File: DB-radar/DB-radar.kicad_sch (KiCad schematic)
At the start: 33 parts, among them J1 Conn_01x10_Female, J2 USB_C_Receptacle, Q1 FS8205A, SW1 SW_Push, U1 ATmega328PB-A, U2 DW01A-G, U3 TP4056, U4 XC6206PxxxMR, Y1 Crystal_GND3_Small

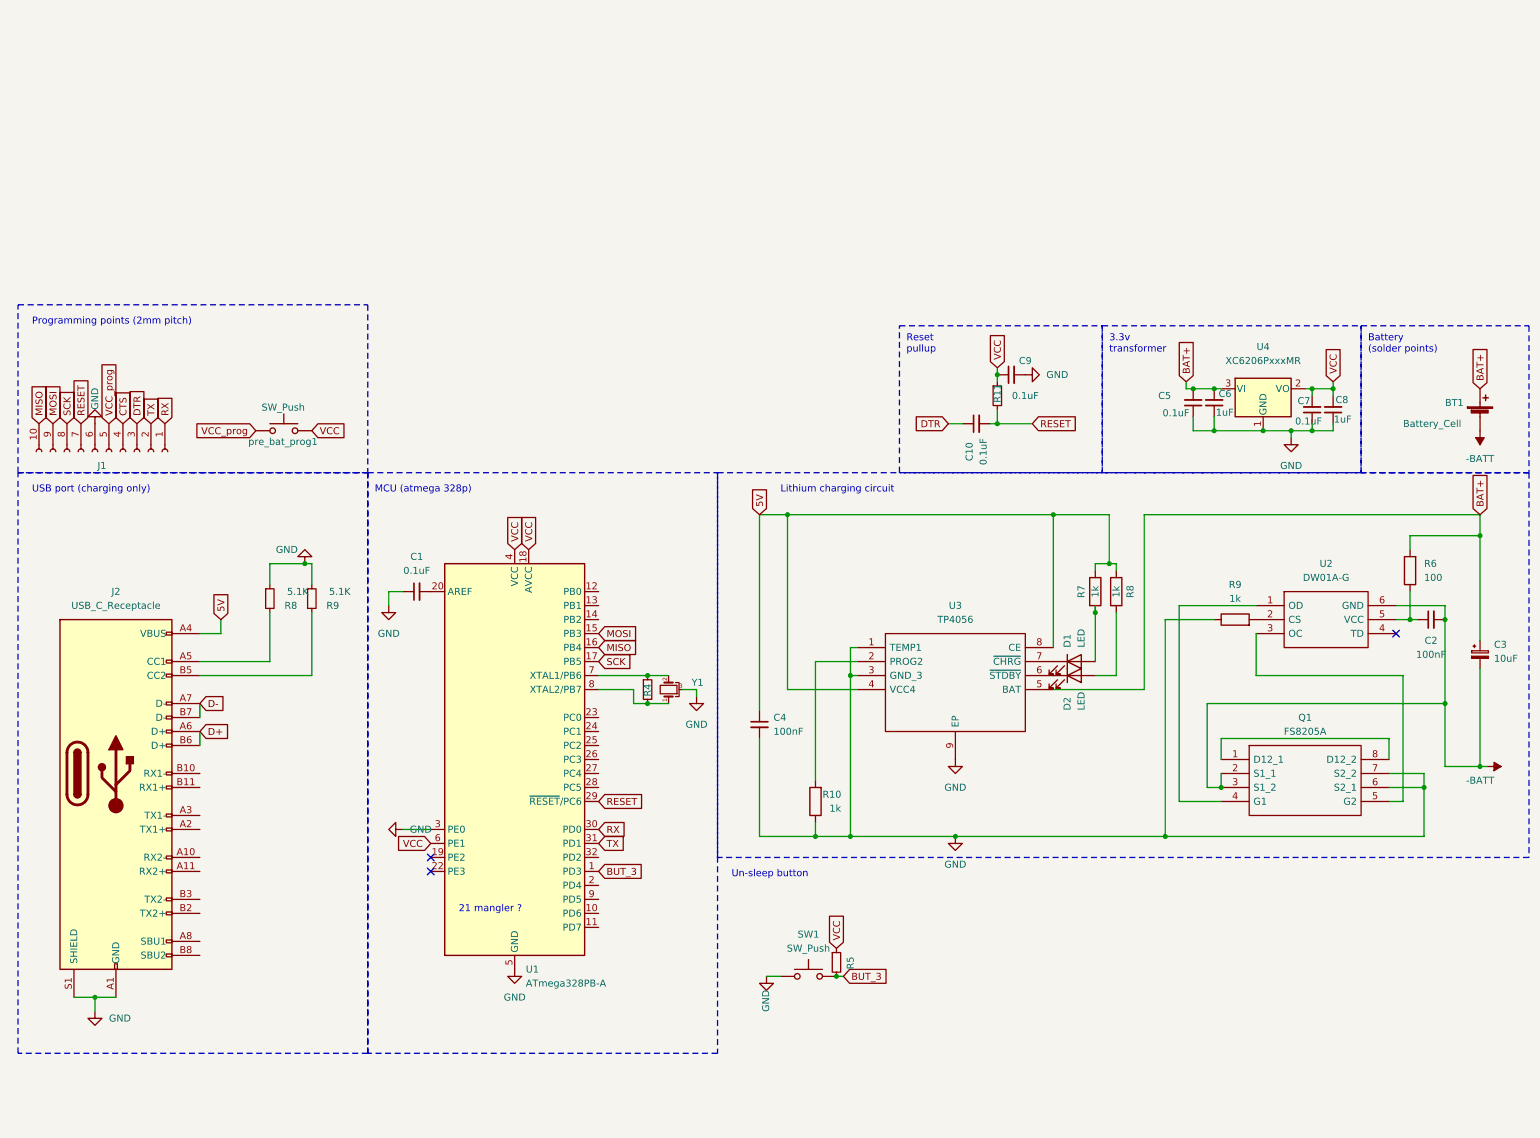
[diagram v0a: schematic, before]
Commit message: Added LED and multiplexers and started PCB design
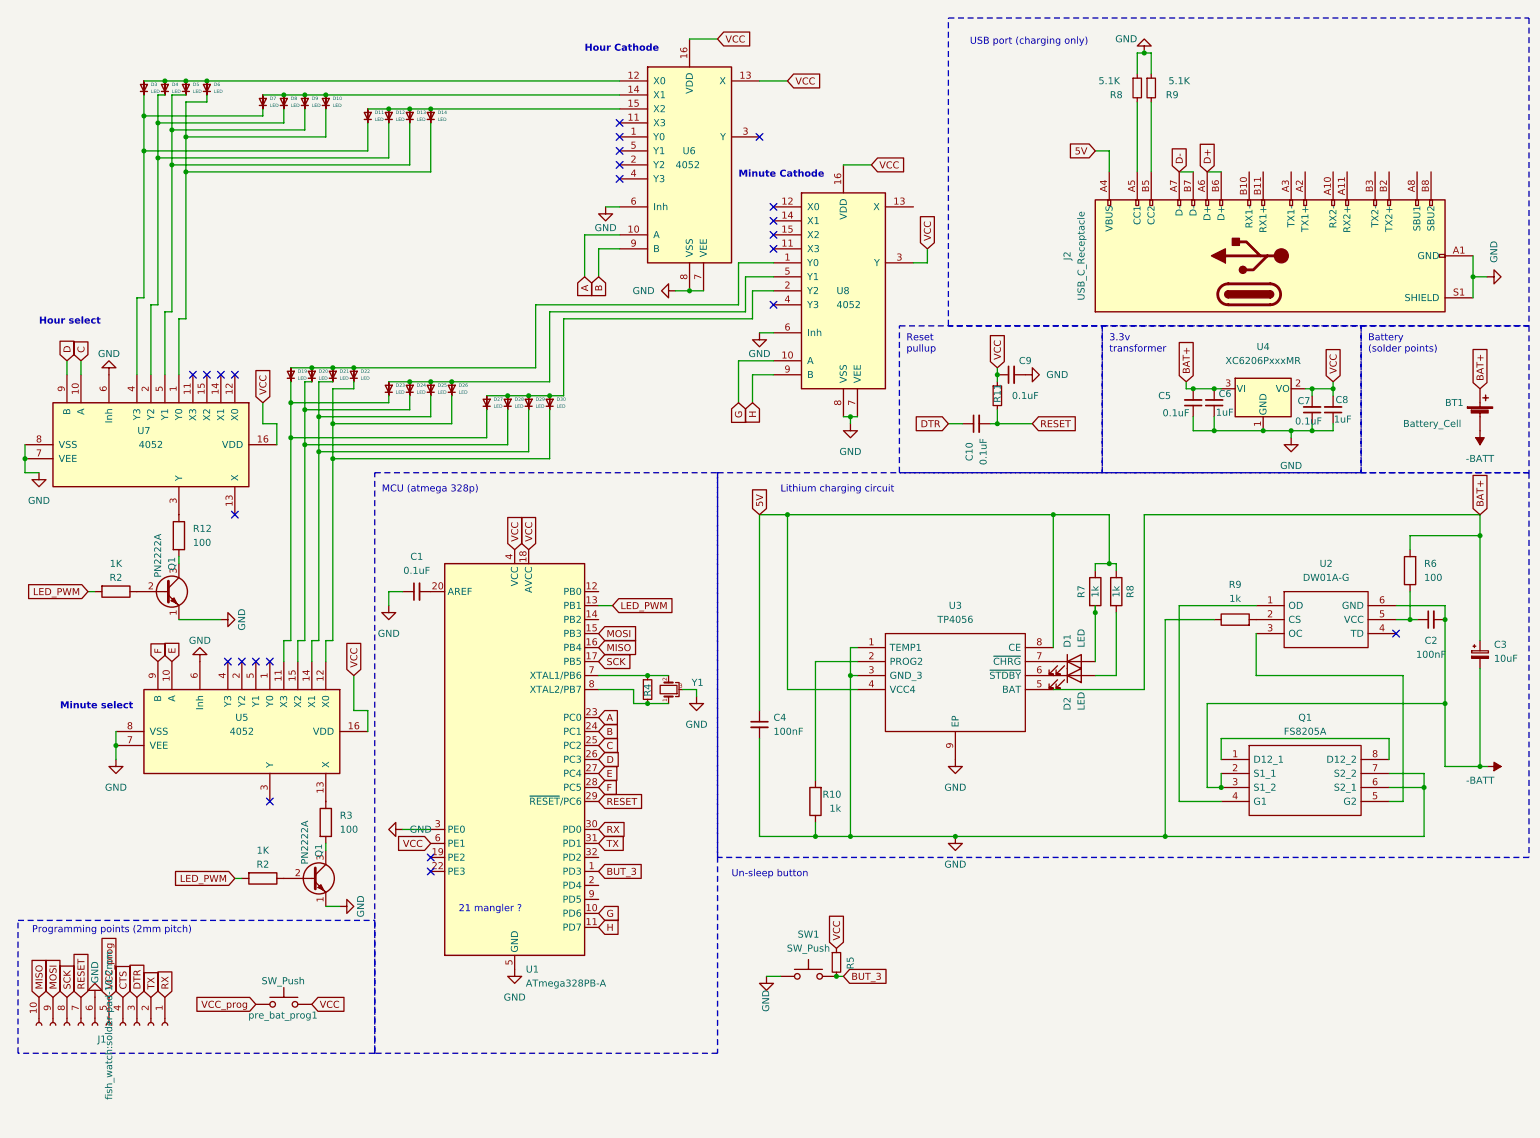
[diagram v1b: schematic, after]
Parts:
- added D10, D11, D12, D13, D14, D19, D20, D21, D22, D23, D24, D25, D26, D27, D28, D29, D3, D30, D4, D5, D6, D7, D8, D9: LED, LED_SMD:LED_0805_2012Metric, symbol Device:LED
- added Q1 (x2): PN2222A, transistorer:MMBT2222A, symbol Transistor_BJT:PN2222A
- added R12, R3: 100, Resistor_SMD:R_0603_1608Metric, symbol Device:R
- added R2 (x2): 1K, Resistor_SMD:R_0603_1608Metric, symbol Device:R
- added U5, U6, U7, U8: 4052, Package_SO:SOIC-16_3.9x9.9mm_P1.27mm, symbol 4xxx:4052
- D1, D2: footprint LED_SMD:LED_0603_1608Metric -> LED_SMD:LED_0805_2012Metric
- J1: footprint fish_watch:solder-pad-10 -> fish_watch:solder-pad-10-2mm
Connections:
- net GND: now also Q1.1 (E), Q1.1 (E), U5.6 (Inh), U5.7 (VEE), U5.8 (VSS), U6.6 (Inh), U6.7 (VEE), U6.8 (VSS), U7.6 (Inh), U7.7 (VEE), U7.8 (VSS), U8.6 (Inh), U8.7 (VEE), U8.8 (VSS)
- net VCC: now also U5.16 (VDD), U6.13 (X), U6.16 (VDD), U7.16 (VDD), U8.16 (VDD), U8.3 (Y)
- net G: now reaches U1.10 (PD6)
- net G: now also U8.10 (A)
- net H: now reaches U1.11 (PD7)
- net H: now also U8.9 (B)
- net LED_PWM: now reaches U1.13 (PB1)
- net LED_PWM: now also R2.2, R2.2
- net A: now reaches U1.23 (PC0)
- net A: now also U6.10 (A)
- net B: now reaches U1.24 (PC1)
- net B: now also U6.9 (B)
- net C: now reaches U1.25 (PC2)
- net C: now also U7.10 (A)
- net D: now reaches U1.26 (PC3)
- net D: now also U7.9 (B)
- net E: now reaches U1.27 (PC4)
- net E: now also U5.10 (A)
- net F: now reaches U1.28 (PC5)
- net F: now also U5.9 (B)
- new net: Q1.2 (B), R2.1 (x2)
- new net: D19.2 (A), D20.2 (A), D21.2 (A), D22.2 (A), U8.1 (Y0)
- new net: D27.2 (A), D28.2 (A), D29.2 (A), D30.2 (A), U8.2 (Y2)
- new net: D23.2 (A), D24.2 (A), D25.2 (A), D26.2 (A), U8.5 (Y1)
- new net: D19.1 (K), D23.1 (K), D27.1 (K), U5.11 (X3)
- new net: D10.1 (K), D14.1 (K), D6.1 (K), U7.1 (Y0)
- new net: D11.2 (A), D12.2 (A), D13.2 (A), D14.2 (A), U6.15 (X2)
- new net: D13.1 (K), D5.1 (K), D9.1 (K), U7.5 (Y1)
- new net: D3.2 (A), D4.2 (A), D5.2 (A), D6.2 (A), U6.12 (X0)
- new net: D11.1 (K), D3.1 (K), D7.1 (K), U7.4 (Y3)
- new net: D10.2 (A), D7.2 (A), D8.2 (A), D9.2 (A), U6.14 (X1)
- new net: D22.1 (K), D26.1 (K), D30.1 (K), U5.12 (X0)
- new net: R3.1, U5.13 (X)
- new net: D21.1 (K), D25.1 (K), D29.1 (K), U5.14 (X1)
- new net: D20.1 (K), D24.1 (K), D28.1 (K), U5.15 (X2)
- new net: R12.1, U7.3 (Y)
- new net: Q1.3 (C), R12.2
- new net: D12.1 (K), D4.1 (K), D8.1 (K), U7.2 (Y2)
- new net: Q1.3 (C), R3.2
- no-connect marks 3 -> 24
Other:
- note added: "Hour Cathode"
- note added: "Hour select"
- note added: "Minute Cathode"
- note added: "Minute select"
- moved on the sheet: J1, J2, R8, R9, pre_bat_prog1

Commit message: De fleste komponenter plassert
Mangler bare et par blokker og routing
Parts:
- removed D2: LED, LED_SMD:LED_0805_2012Metric, symbol Device:LED
- removed R8: 1k, Resistor_SMD:R_0603_1608Metric, symbol Device:R
- removed pre_bat_prog1: SW_Push, Jumper:SolderJumper-2_P1.3mm_Bridged2Bar_RoundedPad1.0x1.5mm, symbol Switch:SW_Push
- added SW2: SW_SPDT, fish_watch:MSK-12C02, symbol Switch:SW_SPDT
- added SW4: SW_MEC_5G, Jumper:SolderJumper-2_P1.3mm_Open_TrianglePad1.0x1.5mm, symbol Switch:SW_MEC_5G
- R10: footprint Resistor_SMD:R_0603_1608Metric -> Resistor_SMD:R_0805_2012Metric_Pad1.20x1.40mm_HandSolder
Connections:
- net BAT+: now also SW4.3 (B), SW4.4 (B)
- net VCC: now also SW2.2 (B); no longer C7.2, C8.2, U4.2 (VO)
- net VCC_prog: now also SW2.1 (A)
- new net: SW4.1 (A), SW4.2 (A)
- new net VCC_bat: C7.2, C8.2, SW2.3 (C), U4.2 (VO)
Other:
- note added: "Solder jumper for å kjøre 3.3 omformer av USB (uten batteri)"
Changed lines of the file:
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@@
-    (stroke (width 0) (type default))
-  )
-  (wire (pts (xy 207.01 130.81) (xy 210.82 130.81))
     (stroke (width 0) (type default))
   )
@@
     (stroke (width 0) (type default))
   )
-  (wire (pts (xy 210.82 130.81) (xy 210.82 119.38))
-    (stroke (width 0) (type default))
-  )
   (wire (pts (xy 82.55 30.48) (xy 82.55 38.1))
     (stroke (width 0) (type default))
@@
   (wire (pts (xy 228.6 78.74) (xy 224.79 78.74))
     (stroke (width 0) (type default))
+  )
+  (rectangle (start 10.16 10.16) (end 30.48 46.99)
+    (stroke (width 0) (type dash))
+    (fill (type none))
   )
   (rectangle (start 171.45 67.31) (end 208.28 93.98)
@@
   )
   (text "Reset\npullup" (at 172.72 72.39 0)
+    (effects (font (size 1.27 1.27)) (justify left bottom))
+  )
+  (text "Solder jumper for \nå kjøre 3.3 \nomformer av USB \n(uten batteri)"
+    (at 12.7 45.72 0)
     (effects (font (size 1.27 1.27)) (justify left bottom))
   )
@@
     )
   )
-  (global_label "VCC" (shape input) (at 64.77 190.5 0) (fields_autoplaced)
-    (effects (font (size 1.27 1.27)) (justify left))
-    (property "Intersheetrefs" "${INTERSHEET_REFS}" (at 70.8117 190.5794 0)
+  (global_label "VCC" (shape input) (at 64.77 187.96 0) (fields_autoplaced)
+    (effects (font (size 1.27 1.27)) (justify left))
+    (property "Intersheetrefs" "${INTERSHEET_REFS}" (at 70.8117 188.0394 0)
       (effects (font (size 1.27 1.27)) (justify left) hide)
     )
@@
     )
   )
+  (global_label "VCC_bat" (shape input) (at 54.61 185.42 180) (fields_autoplaced)
+    (effects (font (size 1.27 1.27)) (justify right))
+    (property "Intersheetrefs" "${INTERSHEET_REFS}" (at 44.0049 185.42 0)
+      (effects (font (size 1.27 1.27)) (justify right) hide)
+    )
+  )
   (global_label "VCC" (shape input) (at 101.6 107.95 90) (fields_autoplaced)
     (effects (font (size 1.27 1.27)) (justify left))
@@
     )
   )
-  (global_label "VCC" (shape input) (at 250.19 77.47 90) (fields_autoplaced)
-    (effects (font (size 1.27 1.27)) (justify left))
-    (property "Intersheetrefs" "${INTERSHEET_REFS}" (at 250.19 70.8562 90)
+  (global_label "VCC_bat" (shape input) (at 250.19 77.47 90) (fields_autoplaced)
+    (effects (font (size 1.27 1.27)) (justify left))
+    (property "Intersheetrefs" "${INTERSHEET_REFS}" (at 250.19 66.8649 90)
       (effects (font (size 1.27 1.27)) (justify left) hide)
     )
@@
     (effects (font (size 1.27 1.27)) (justify left))
     (property "Intersheetrefs" "${INTERSHEET_REFS}" (at 121.0952 173.99 0)
+      (effects (font (size 1.27 1.27)) (justify left) hide)
+    )
+  )
+  (global_label "BAT+" (shape input) (at 20.32 20.32 90) (fields_autoplaced)
+    (effects (font (size 1.27 1.27)) (justify left))
+    (property "Intersheetrefs" "${INTERSHEET_REFS}" (at 20.32 12.4362 90)
       (effects (font (size 1.27 1.27)) (justify left) hide)
     )
@@
         (path "/b1ef8062-d0b2-45f0-be8f-ceb4fd46a2d8"
           (reference "R1") (unit 1)
-        )
-      )
-    )
-  )
-  (symbol (lib_id "Switch:SW_Push") (at 59.69 190.5 0) (unit 1)
-    (in_bom yes) (on_board yes) (dnp no)
-    (property "Reference" "pre_bat_prog1" (at 59.5318 192.4976 0)
-      (effects (font (size 1.27 1.27)))
-    )
-    (property "Value" "SW_Push" (at 59.577 186.2606 0)
-      (effects (font (size 1.27 1.27)))
-    )
-    (property "Footprint" "Jumper:SolderJumper-2_P1.3mm_Bridged2Bar_RoundedPad1.0x1.5mm" (at 59.69 185.42 0)
-      (effects (font (size 1.27 1.27)) hide)
-    )
-    (property "Datasheet" "~" (at 59.69 185.42 0)
-      (effects (font (size 1.27 1.27)) hide)
-    )
-    (pin "1")
-    (pin "2")
-    (instances
-      (project "DB-radar"
-        (path "/4fe367bb-912f-4df7-b060-07157080bb20"
-          (reference "pre_bat_prog1") (unit 1)
-        )
-      )
-      (project "fish clock"
-        (path "/8a39ddf7-266a-4e35-8762-e2f31a43cf6c"
-          (reference "pre_bat_prog1") (unit 1)
         )
       )
@@
     )
   )
-  (symbol (lib_id "Device:R") (at 210.82 115.57 0) (unit 1)
-    (in_bom yes) (on_board yes) (dnp no)
-    (property "Reference" "R8" (at 213.36 115.57 90)
-      (effects (font (size 1.27 1.27)))
-    )
-    (property "Value" "1k" (at 210.82 115.57 90)
-      (effects (font (size 1.27 1.27)))
-    )
-    (property "Footprint" "Resistor_SMD:R_0603_1608Metric" (at 209.042 115.57 90)
-      (effects (font (size 1.27 1.27)) hide)
-    )
-    (property "Datasheet" "~" (at 210.82 115.57 0)
-      (effects (font (size 1.27 1.27)) hide)
-    )
-    (pin "1")
-    (pin "2")
-    (instances
-      (project "DB-radar"
-        (path "/4fe367bb-912f-4df7-b060-07157080bb20"
-          (reference "R8") (unit 1)
-        )
-      )
-      (project "fish clock"
-        (path "/8a39ddf7-266a-4e35-8762-e2f31a43cf6c"
-          (reference "R30") (unit 1)
-        )
-      )
-    )
-  )
   (symbol (lib_id "power:GND") (at 29.21 146.05 0) (unit 1)
     (in_bom yes) (on_board yes) (dnp no) (fields_autoplaced)
@@
     )
     (property "Footprint" "fish_watch:solder-pad-10-2mm" (at 27.94 194.31 0)
-      (effects (font (size 1.27 1.27)))
+      (effects (font (size 1.27 1.27)) hide)
     )
     (property "Datasheet" "~" (at 27.94 194.31 0)
@@
     )
   )
+  (symbol (lib_id "Switch:SW_SPDT") (at 59.69 187.96 180) (unit 1)
+    (in_bom yes) (on_board yes) (dnp no) (fields_autoplaced)
+    (property "Reference" "SW2" (at 59.69 180.34 0)
+      (effects (font (size 1.27 1.27)))
+    )
+    (property "Value" "SW_SPDT" (at 59.69 182.88 0)
+      (effects (font (size 1.27 1.27)))
+    )
+    (property "Footprint" "fish_watch:MSK-12C02" (at 59.69 187.96 0)
+      (effects (font (size 1.27 1.27)) hide)
+    )
+    (property "Datasheet" "~" (at 59.69 187.96 0)
+      (effects (font (size 1.27 1.27)) hide)
+    )
+    (pin "1")
+    (pin "2")
+    (pin "3")
+    (instances
+      (project "DB-radar"
+        (path "/4fe367bb-912f-4df7-b060-07157080bb20"
+          (reference "SW2") (unit 1)
+        )
+      )
+    )
+  )
   (symbol (lib_id "Device:R") (at 156.21 153.67 180) (unit 1)
     (in_bom yes) (on_board yes) (dnp no)
@@
       (effects (font (size 1.27 1.27)) (justify right))
     )
-    (property "Footprint" "Resistor_SMD:R_0603_1608Metric" (at 157.988 153.67 90)
+    (property "Footprint" "Resistor_SMD:R_0805_2012Metric_Pad1.20x1.40mm_HandSolder" (at 157.988 153.67 90)
       (effects (font (size 1.27 1.27)) hide)
     )
@@
         (path "/b1ef8062-d0b2-45f0-be8f-ceb4fd46a2d8"
           (reference "Q1") (unit 1)
+        )
+      )
+    )
+  )
+  (symbol (lib_id "Switch:SW_MEC_5G") (at 20.32 25.4 90) (unit 1)
+    (in_bom yes) (on_board yes) (dnp no) (fields_autoplaced)
+    (property "Reference" "SW4" (at 21.59 24.13 90)
+      (effects (font (size 1.27 1.27)) (justify right))
+    )
+    (property "Value" "SW_MEC_5G" (at 21.59 26.67 90)
+      (effects (font (size 1.27 1.27)) (justify right) hide)
+    )
+    (property "Footprint" "Jumper:SolderJumper-2_P1.3mm_Open_TrianglePad1.0x1.5mm" (at 15.24 25.4 0)
+      (effects (font (size 1.27 1.27)) hide)
+    )
+    (property "Datasheet" "http://www.apem.com/int/index.php?controller=attachment&id_attachment=488" (at 15.24 25.4 0)
+      (effects (font (size 1.27 1.27)) hide)
+    )
+    (pin "3")
+    (pin "4")
+    (pin "1")
+    (pin "2")
+    (instances
+      (project "DB-radar"
+        (path "/4fe367bb-912f-4df7-b060-07157080bb20"
+          (reference "SW4") (unit 1)
         )
       )
@@
         )
       )
-    )
-  )
-  (symbol (lib_id "Device:LED") (at 203.2 130.81 0) (unit 1)
-    (in_bom yes) (on_board yes) (dnp no)
-    (property "Reference" "D2" (at 201.93 137.16 90)
-      (effects (font (size 1.27 1.27)) (justify left))
-    )
-    (property "Value" "LED" (at 204.47 137.16 90)
-      (effects (font (size 1.27 1.27)) (justify left))
-    )
-    (property "Footprint" "LED_SMD:LED_0805_2012Metric" (at 203.2 130.81 0)
-      (effects (font (size 1.27 1.27)) hide)
-    )
-    (property "Datasheet" "~" (at 203.2 130.81 0)
-      (effects (font (size 1.27 1.27)) hide)
-    )
-    (pin "1")
-    (pin "2")
-    (instances
-      (project "DB-radar"
-        (path "/4fe367bb-912f-4df7-b060-07157080bb20"
-          (reference "D2") (unit 1)
-        )
-      )
-      (project "fish clock"
-        (path "/8a39ddf7-266a-4e35-8762-e2f31a43cf6c"
-          (reference "D6") (unit 1)
-        )
-      )

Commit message: Begynnt å route
Mega-rotete
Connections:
- net 5V: now also SW4.1 (A)
- net BAT+: now also SW4.2 (B); no longer SW4.3 (B), SW4.4 (B)
- net VCC_bat: now also SW2.1 (A); no longer SW2.3 (C)
- net VCC_prog: now also SW2.3 (C); no longer SW2.1 (A)
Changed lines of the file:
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@@
     )
   )
-  (global_label "VCC_prog" (shape input) (at 54.61 190.5 180) (fields_autoplaced)
+  (global_label "VCC_prog" (shape input) (at 54.61 185.42 180) (fields_autoplaced)
     (effects (font (size 1.27 1.27)) (justify right))
-    (property "Intersheetrefs" "${INTERSHEET_REFS}" (at 42.7954 190.5 0)
+    (property "Intersheetrefs" "${INTERSHEET_REFS}" (at 42.7954 185.42 0)
       (effects (font (size 1.27 1.27)) (justify right) hide)
     )
@@
     )
   )
-  (global_label "VCC_bat" (shape input) (at 54.61 185.42 180) (fields_autoplaced)
+  (global_label "VCC_bat" (shape input) (at 54.61 190.5 180) (fields_autoplaced)
     (effects (font (size 1.27 1.27)) (justify right))
-    (property "Intersheetrefs" "${INTERSHEET_REFS}" (at 44.0049 185.42 0)
+    (property "Intersheetrefs" "${INTERSHEET_REFS}" (at 44.0049 190.5 0)
       (effects (font (size 1.27 1.27)) (justify right) hide)
     )
@@
     (property "Intersheetrefs" "${INTERSHEET_REFS}" (at 121.0952 173.99 0)
       (effects (font (size 1.27 1.27)) (justify left) hide)
+    )
+  )
+  (global_label "5V" (shape input) (at 20.32 30.48 270) (fields_autoplaced)
+    (effects (font (size 1.27 1.27)) (justify right))
+    (property "Intersheetrefs" "${INTERSHEET_REFS}" (at 20.32 35.7633 90)
+      (effects (font (size 1.27 1.27)) (justify right) hide)
     )
   )
@@
       (effects (font (size 1.27 1.27)) hide)
     )
-    (pin "3")
-    (pin "4")
-    (pin "1")
-    (pin "2")
+    (pin "1")
+    (pin "2")
